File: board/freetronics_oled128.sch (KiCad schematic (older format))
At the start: 38 parts, among them IC1 TPS61040, P1 M02X05, P2 MICROSD, P3 M02X02, P4 M02X02, Q1 2N7002, SW1 SW_PUSHBUTTON, SW2 SW_PUSHBUTTON, U1 MC74VHCT50A

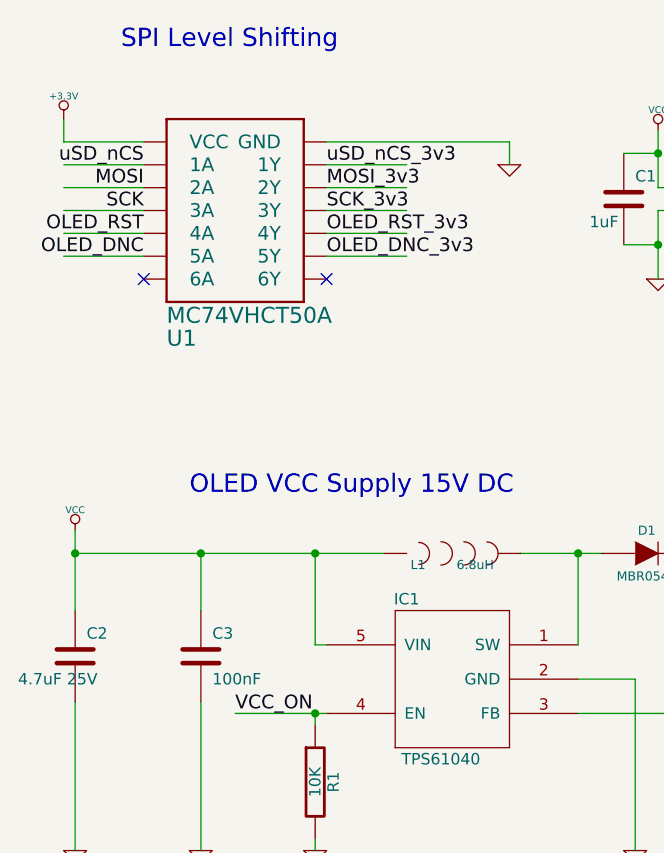
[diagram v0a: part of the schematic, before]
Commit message: Change C2 filter from 4.7uF 25V to 10uF 16V
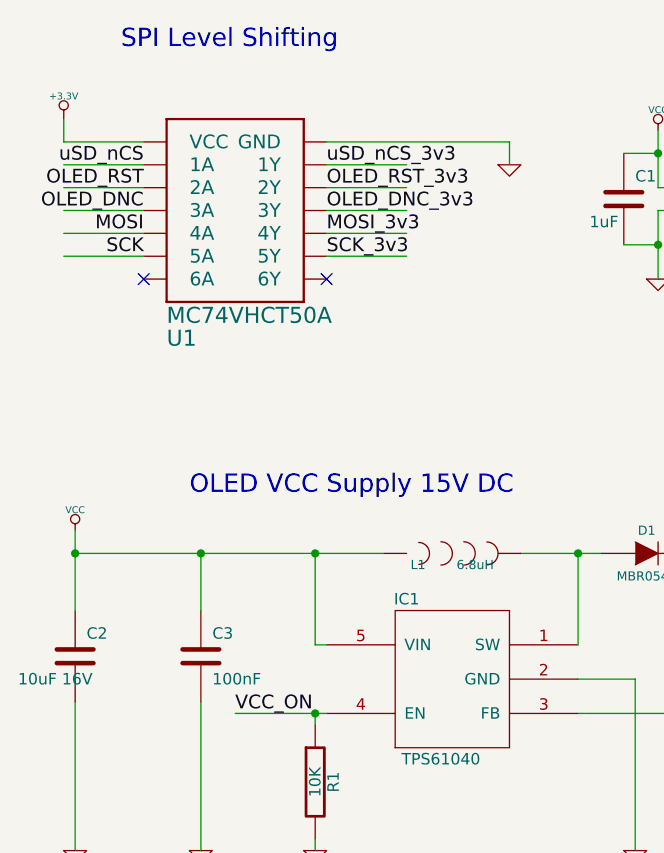
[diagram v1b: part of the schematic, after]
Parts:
- C2: value 4.7uF 25V -> 10uF 16V
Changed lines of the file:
@@
-EESchema Schematic File Version 2  date Wed 08 May 2013 09:40:02 EST
+EESchema Schematic File Version 2  date Wed 08 May 2013 10:47:16 EST
 LIBS:freetronics_kicad_sch_lib
 LIBS:power
@@
 Sheet 1 1
 Title "Freetronics OLED128              http://www.freetronics.com/oled128"
-Date "7 may 2013"
+Date "8 may 2013"
 Rev "1.2"
 Comp "(C)2013 Freetronics Pty Ltd"
@@
 Text Notes 1350 3350 0    80   ~ 0
 SPI Level Shifting
-Text Label 2250 4050 0    60   ~ 0
+Text Label 2250 4250 0    60   ~ 0
 SCK_3v3
 Text Label 9250 2450 0    60   ~ 0
@@
 P 1150 6000
 F 0 "C2" H 1200 6100 50  0000 L CNN
-F 1 "4.7uF  25V" H 900 5900 50  0000 L CNN
+F 1 "10uF  16V" H 900 5900 50  0000 L CNN
 F 2 "" H 1150 6000 60  0001 C CNN
 F 3 "" H 1150 6000 60  0001 C CNN
@@
 	1    0    0    -1
 $EndComp
+Text Label 1450 3950 2    60   ~ 0
+OLED_RST
+Text Label 1450 4050 2    60   ~ 0
+OLED_DNC
+Text Label 1450 4250 2    60   ~ 0
+SCK
 Text Label 1450 4150 2    60   ~ 0
-OLED_RST
-Text Label 1450 4250 2    60   ~ 0
-OLED_DNC
-Text Label 1450 4050 2    60   ~ 0
-SCK
-Text Label 1450 3950 2    60   ~ 0
 MOSI
 $Comp
@@
 	1    0    0    -1
 $EndComp
-Text Label 2250 3950 0    60   ~ 0
+Text Label 2250 4150 0    60   ~ 0
 MOSI_3v3
 Wire Wire Line
@@
 Text Label 9700 3150 2    60   ~ 0
 OLED_RST_3v3
-Text Label 2250 4250 0    60   ~ 0
+Text Label 2250 4050 0    60   ~ 0
 OLED_DNC_3v3
-Text Label 2250 4150 0    60   ~ 0
+Text Label 2250 3950 0    60   ~ 0
 OLED_RST_3v3
 $Comp

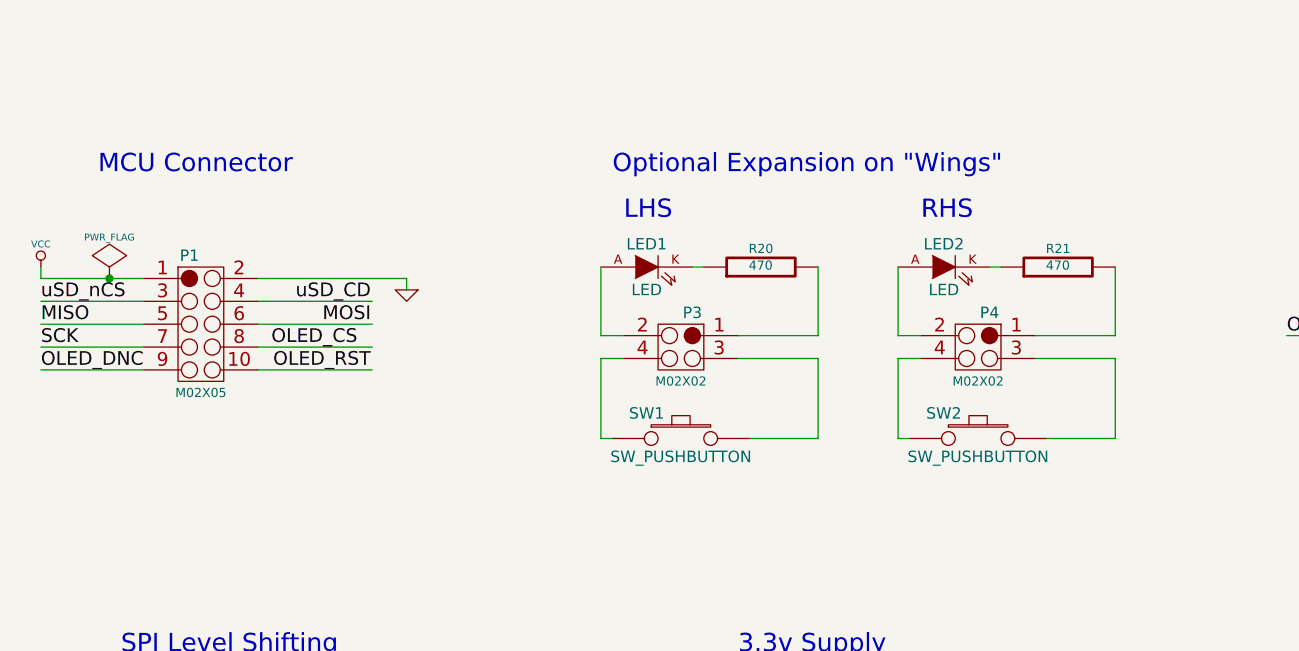
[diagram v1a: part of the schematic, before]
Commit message: Add notes on the schematic about common Arduino SPI pin numbers
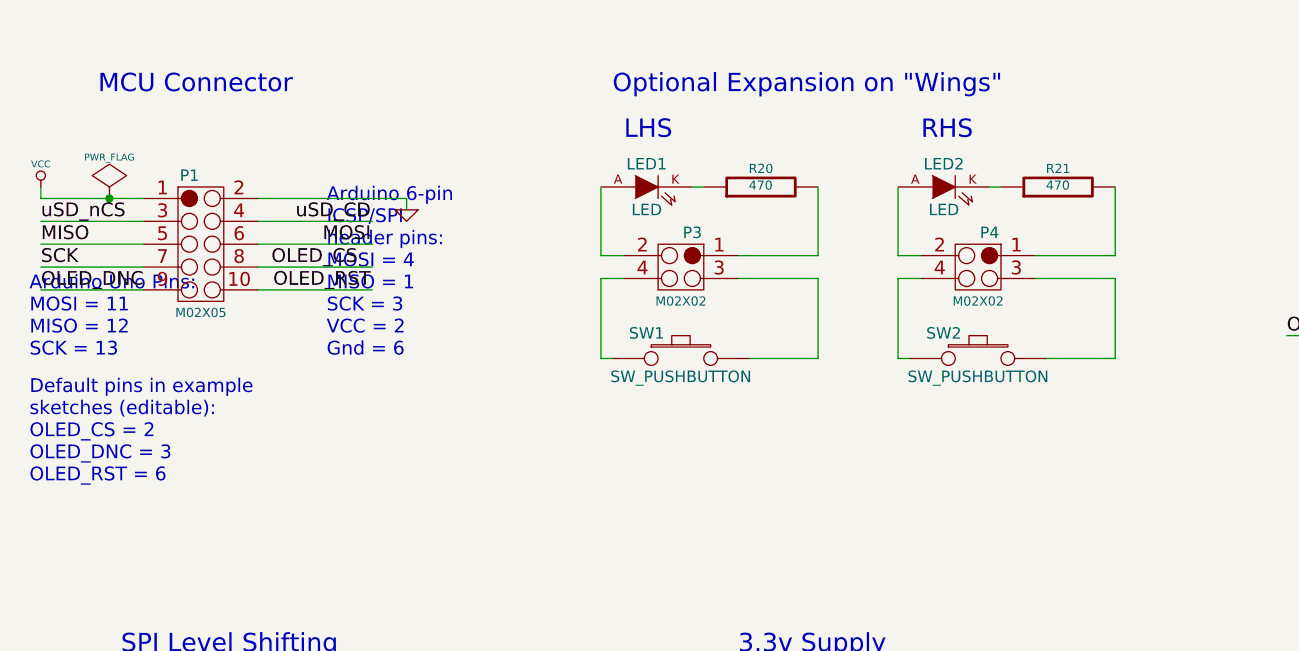
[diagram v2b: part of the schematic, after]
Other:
- note added: "Arduino 6-pin\nICSP/SPI\nheader pins:\nMOSI = 4\nMISO = 1\nSCK = 3\nVCC = 2\nGnd = 6"
- note added: "Arduino Uno Pins:\nMOSI = 11\nMISO = 12\nSCK = 13"
- note added: "Default pins in example\nsketches (editable):\nOLED_CS = 2\nOLED_DNC = 3\nOLED_RST = 6"
- moved on the sheet: LED1, LED2, P1, P3, P4, R20, R21, SW1, SW2

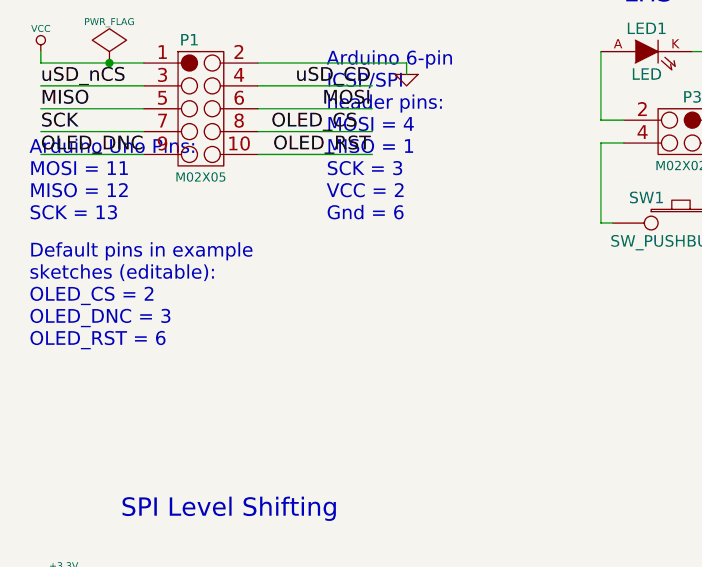
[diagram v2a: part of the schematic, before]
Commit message: Add note about default uSD nCS pin to schematic
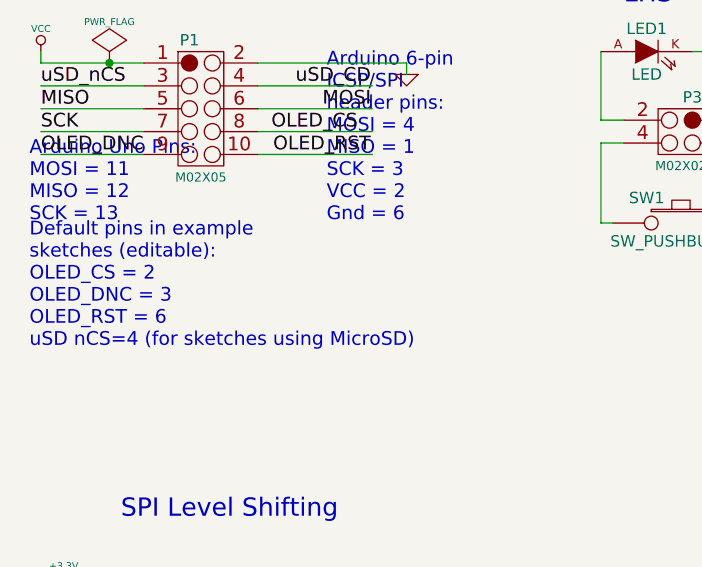
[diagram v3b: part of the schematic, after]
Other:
- note added: "Default pins in example\nsketches (editable):\nOLED_CS = 2\nOLED_DNC = 3\nOLED_RST = 6\nuSD nCS=4 (for sketches using MicroSD)"
- note removed: "Default pins in example\nsketches (editable):\nOLED_CS = 2\nOLED_DNC = 3\nOLED_RST = 6"
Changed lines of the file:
@@
-EESchema Schematic File Version 2  date Wed 08 May 2013 11:16:51 EST
+EESchema Schematic File Version 2  date Thu 09 May 2013 17:07:11 EST
 LIBS:freetronics_kicad_sch_lib
 LIBS:power
@@
 Sheet 1 1
 Title "Freetronics OLED128              http://www.freetronics.com/oled128"
-Date "8 may 2013"
+Date "9 may 2013"
 Rev "1.2"
 Comp "(C)2013 Freetronics Pty Ltd"
@@
 Arduino 6-pin\nICSP/SPI\nheader pins:\nMOSI = 4\nMISO = 1\nSCK = 3\nVCC = 2\nGnd = 6
 Text Notes 950  2600 0    60   ~ 0
-Default pins in example\nsketches (editable):\nOLED_CS = 2\nOLED_DNC = 3\nOLED_RST = 6
+Default pins in example\nsketches (editable):\nOLED_CS = 2\nOLED_DNC = 3\nOLED_RST = 6\nuSD nCS=4 (for sketches using MicroSD)
 $EndSCHEMATC
